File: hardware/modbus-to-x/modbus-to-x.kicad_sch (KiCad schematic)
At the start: 33 parts, among them J1 PWR, J2 UART, SW1 SW_Push, SW2 SW_Push, U1 AMS1117-3.3, U3 MAX3485, U4 ESP32-WROOM-32D, U5 AT24CS64-XHM, U6 AT24CS64-XHM, U7 LMR14020SQDPRTQ1

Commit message: updated hw
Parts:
- removed C1: 4.7uF/25V, Capacitor_SMD:C_0805_2012Metric_Pad1.18x1.45mm_HandSolder, symbol Device:C
- removed C12: 47uF, ~, symbol SparkFun-Capacitor:C_Polarized
- removed C9: 22uF/10V(20%), Capacitor_SMD:C_0402_1005Metric_Pad0.74x0.62mm_HandSolder, symbol Device:C
- added C1: 47uF, Capacitor_SMD:CP_Elec_6.3x5.4, symbol Device:C_Polarized
- added C12, C21: 100pF, Capacitor_SMD:C_0805_2012Metric_Pad1.18x1.45mm_HandSolder, symbol Device:C
- added C13, C14, C16, C17, C18, C2: 10uF, Capacitor_SMD:C_0805_2012Metric_Pad1.18x1.45mm_HandSolder, symbol Device:C
- added C15: 22uF, Capacitor_SMD:C_0805_2012Metric_Pad1.18x1.45mm_HandSolder, symbol Device:C
- added C19: 0.01uF, Capacitor_SMD:C_0402_1005Metric_Pad0.74x0.62mm_HandSolder, symbol Device:C
- added C20: 2.2nF, Capacitor_SMD:C_0805_2012Metric_Pad1.18x1.45mm_HandSolder, symbol Device:C
- added C22: 0.1uF, Capacitor_SMD:C_1206_3216Metric_Pad1.33x1.80mm_HandSolder, symbol Device:C
- added D3: SMAJ12A, Diode_SMD:D_SMA_Handsoldering, symbol Diode:SMAJ12A
- added L2: MPZ1005S121CT000, MPZ1005S121CT000:IND_1005_TDK-L, symbol MPZ1005S121CT000:MPZ1005S121CT000
- added R10: 47k, Resistor_SMD:R_0805_2012Metric_Pad1.20x1.40mm_HandSolder, symbol Device:R
- added R11: 22K, Resistor_SMD:R_0603_1608Metric_Pad0.98x0.95mm_HandSolder, symbol Device:R
- added R12: 620R, Resistor_SMD:R_0805_2012Metric_Pad1.20x1.40mm_HandSolder, symbol Device:R
- C10: FriendlyName (none) -> CBoot; PartNo (none) -> CC0402MRX5R7BB104; Voltage (none) -> 16V
- C11: value 4.7uF -> 2.2nF; footprint Capacitor_SMD:C_0402_1005Metric_Pad0.74x0.62mm_HandSolder -> Capacitor_SMD:C_0805_2012Metric_Pad1.18x1.45mm_HandSolder; FriendlyName (none) -> Css; PartNo (none) -> RND 1500805B222J500NT; Voltage (none) -> 50V
- C3: value 0.1uF/50V(10%) -> 22uF; footprint Capacitor_SMD:C_0402_1005Metric_Pad0.74x0.62mm_HandSolder -> Capacitor_SMD:C_0805_2012Metric_Pad1.18x1.45mm_HandSolder; ProductCode (none) -> CL21A226MOCLRNC; now left out of the parts list
- C4, C5, C7: value 0.1uF/50V(10%) -> 0.1uF; footprint Capacitor_SMD:C_0402_1005Metric_Pad0.74x0.62mm_HandSolder -> Capacitor_SMD:C_1206_3216Metric_Pad1.33x1.80mm_HandSolder; ProductCode (none) -> CVNF100K12X; now left out of the parts list
- C6, C8: value 22uF/10V(20%) -> 22uF; footprint Capacitor_SMD:C_0402_1005Metric_Pad0.74x0.62mm_HandSolder -> Capacitor_SMD:C_0805_2012Metric_Pad1.18x1.45mm_HandSolder; ProductCode (none) -> CL21A226MOCLRNC; now left out of the parts list
- D1, J1, J2, R2, R3, R4, R5, SW1, SW2, U1, U3, U4, U5, U6: now left out of the parts list
- D2: value MBR0530 -> MBRS340T3G; footprint Diode_SMD:D_SOD-123 -> Diode_SMD:D_SMB-SMC_Universal_Handsoldering; PartNo (none) -> MBRS340T3G
- L1: value 5.5uH -> 4.7uH; footprint SparkFun-Capacitor:C_0805_2012Metric -> WE 74404041047:L_Wurth_WE-LQS-4012; PROD_ID NDUC- -> (none); PartNo (none) -> WE 74404041047
- R1: footprint (none) -> Resistor_SMD:R_1206_3216Metric_Pad1.30x1.75mm_HandSolder; ProductCode (none) -> 1551206S4F1000T5E; now left out of the parts list
- R6: PartNo (none) -> 155TC0525B1002T5J
- R7: value 23.2K -> 620R; FriendlyName (none) -> Rt; PartNo (none) -> 1550805S8F6200T5E
- R8: value 10K -> 390k; footprint Resistor_SMD:R_0805_2012Metric_Pad1.20x1.40mm_HandSolder -> Resistor_SMD:R_0402_1005Metric_Pad0.72x0.64mm_HandSolder; FriendlyName (none) -> Rfbt
- R9: value 10K -> 22k; footprint Resistor_SMD:R_0805_2012Metric_Pad1.20x1.40mm_HandSolder -> Resistor_SMD:R_0603_1608Metric_Pad0.98x0.95mm_HandSolder; FriendlyName (none) -> Rfbb2
- U7: footprint DPR0010A -> LMR14020SQDPRTQ1:DPR0010A
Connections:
- net EN: now also C4.1, C22.1; no longer C3.2, C5.2
- net GND: now also C3.2, C4.2, C5.2, R9.1, C1.2, C13.1, C14.1, C15.1, C16.1, C17.1, C18.1, C19.2, C2.1, C20.1, C22.2, D3.2 (A2), R11.1; no longer C3.1, C4.1, C5.1, R7.1
- net IO_0: now also C5.1; no longer C4.2
- net VBUS_12: now also U7.4 (EN), C1.1, C16.2, C17.2, C18.2, C19.1, L2.1; no longer J1.1 (Pin_1)
- net VCC5: now also C12.2, C13.2, C14.2, C15.2, C2.2, C21.2
- net VDD33: now also C3.1
- net at U7.5 (RT_SYNC): now also R12.1; no longer R7.2
- net at C11.2, U7.6 (SS): now also C20.2
- net at U7.7 (FB): now also R8.2, C12.1, C21.1, R10.2; no longer R9.1
- net at R9.2: now also R10.1; no longer R8.2
- new net: D3.1 (A1), J1.1 (Pin_1), L2.2
- new net: R12.2, R7.2
- new net: R11.2, R7.1
- no-connect marks 29 -> 28
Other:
- note added: "12V Input"
- note added: "3v3 Linear Voltage Regulator"
- note added: "Cff"
- note added: "Cin Caps"
- note added: "Cout Caps"
- note added: "Css"
- note added: "Rfbb"
- note added: "Rt"
- note added: "UART"
- note removed: "Peripherals"
- moved on the sheet: C6, C7, C8, D1, D2, J1, J2, L1, R1, R2, R3, R4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

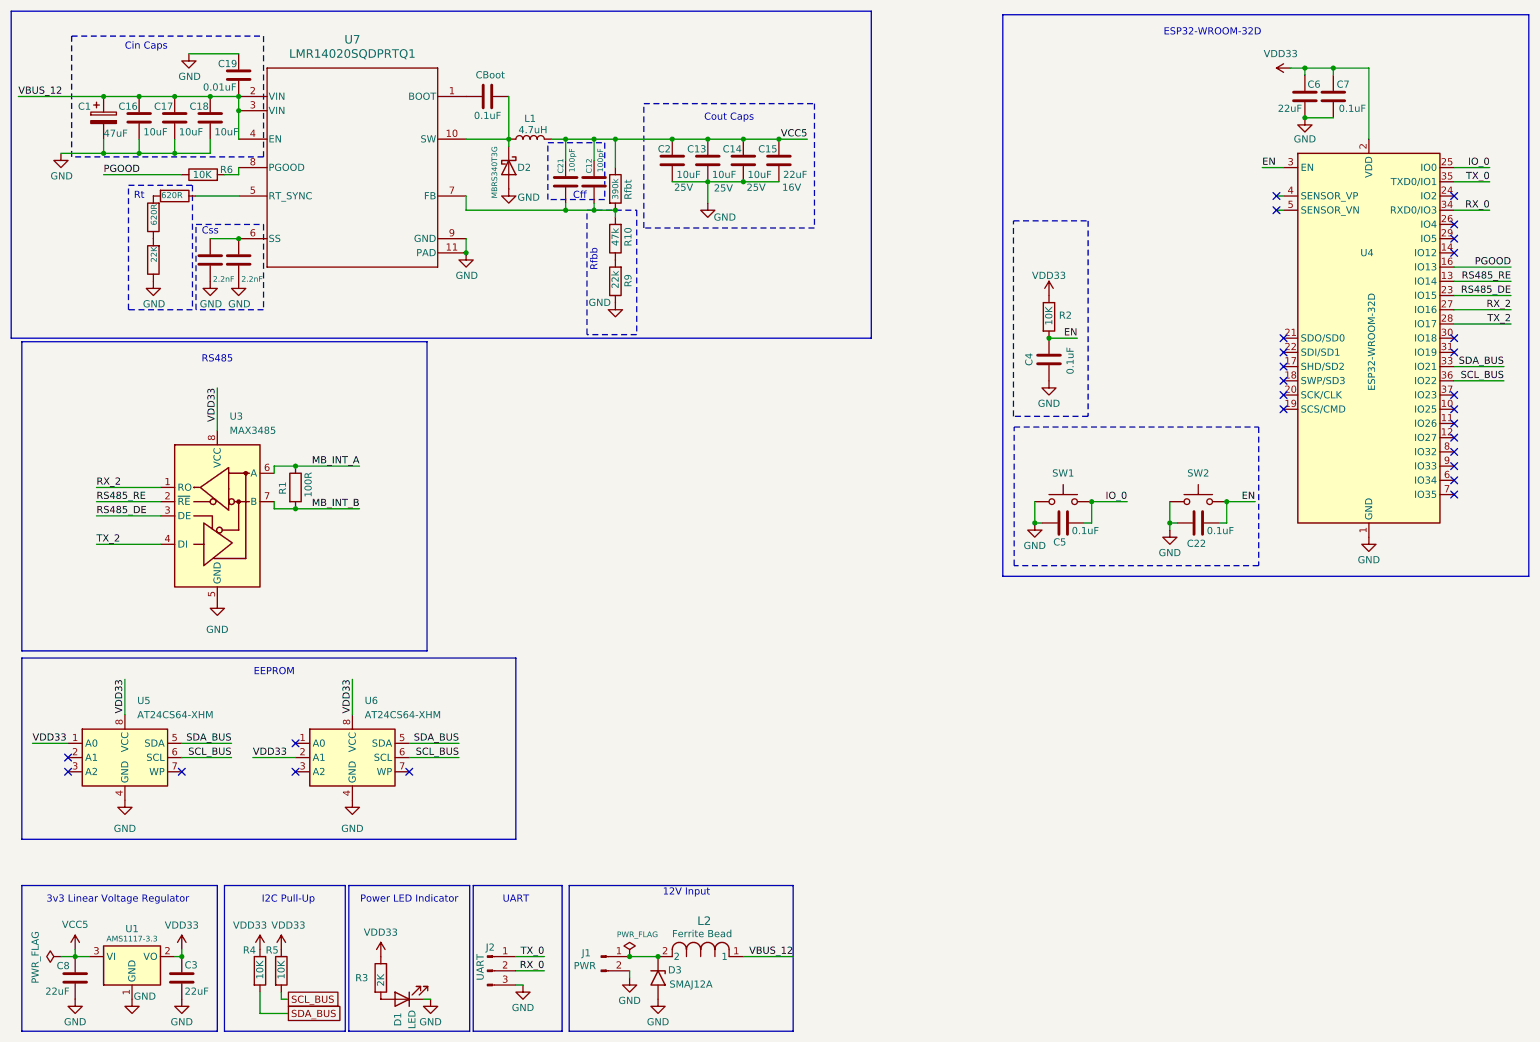
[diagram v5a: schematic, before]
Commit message: updated footprints
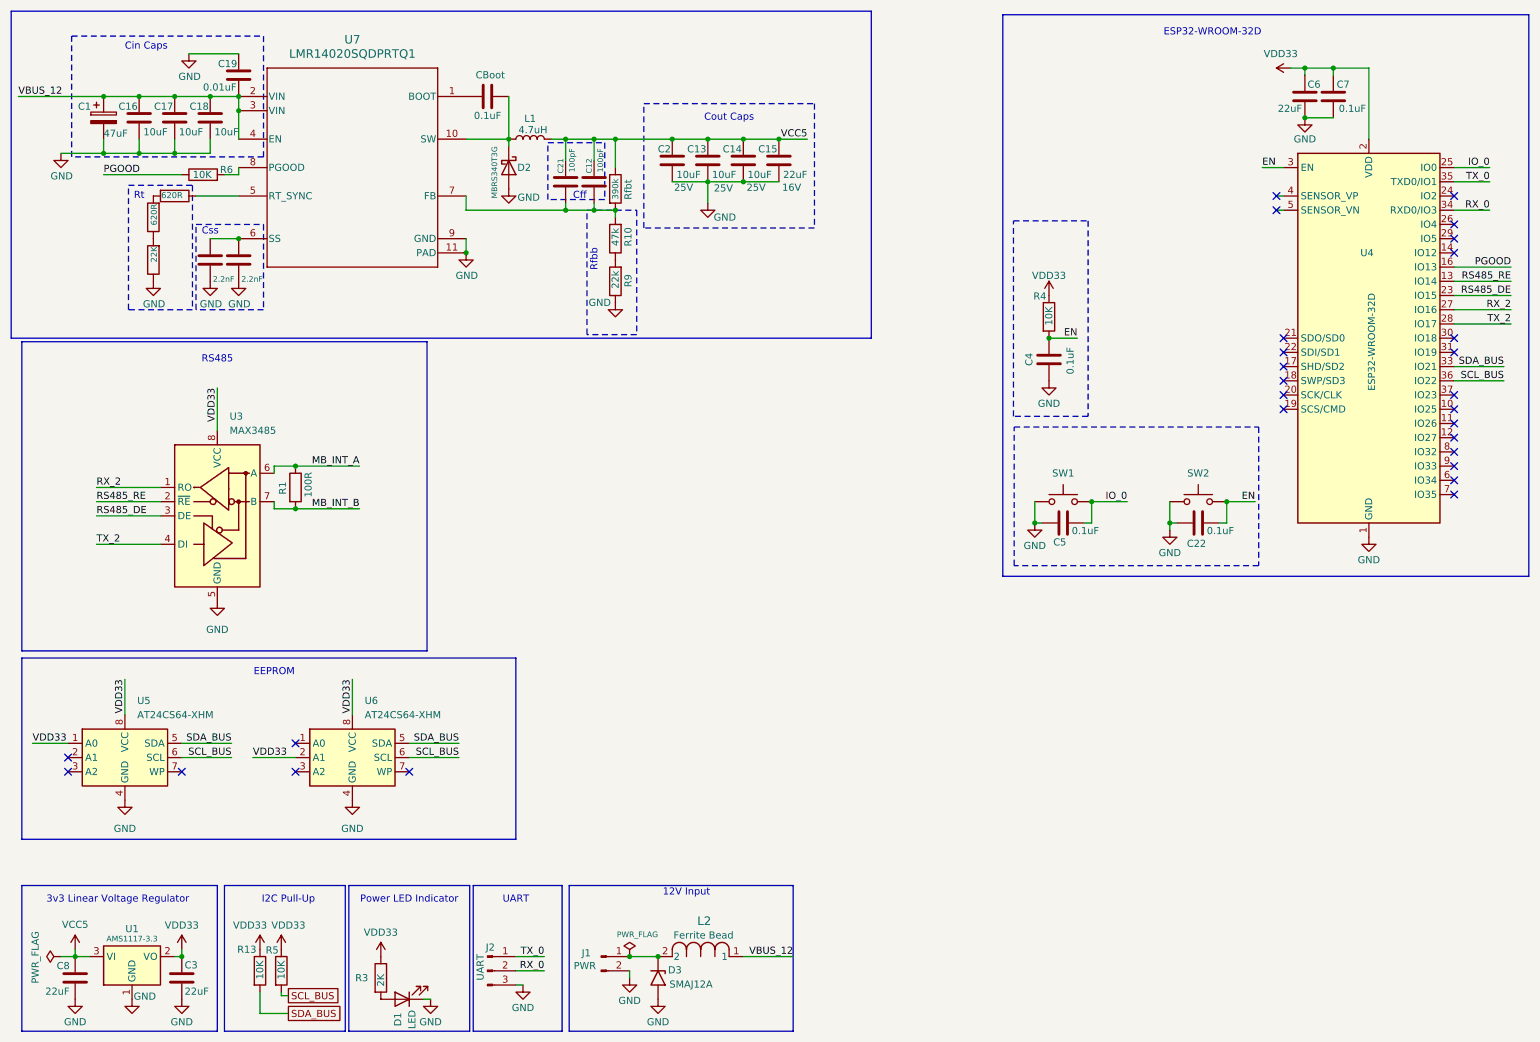
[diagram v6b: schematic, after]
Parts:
- removed R2: 10K, Resistor_SMD:R_0805_2012Metric_Pad1.20x1.40mm_HandSolder, symbol Device:R
- added R13: 10K, Resistor_SMD:R_0805_2012Metric_Pad1.20x1.40mm_HandSolder, symbol Device:R
- C1: FriendlyName (none) -> Cout47uf; PartNo (none) -> CSMK047/35; ProductCode CSMK047/35 -> (none)
- C12: FriendlyName Cff2 -> Cff; PartNo (none) -> RND 1500805N101J500NT; ProductCode RND 1500805N101J500NT -> (none)
- C13, C14, C16, C17, C18, C2: FriendlyName Cout -> Cout10uf
- C15: FriendlyName Cout -> Cout22uf
- C19: FriendlyName Cout -> Cin0_1uf
- C21: FriendlyName Cff1 -> Cff; PartNo (none) -> RND 1500805N101J500NT; ProductCode RND 1500805N101J500NT -> (none)
- C22, C4, C5, C7: PartNo (none) -> CVNF100K12X; ProductCode CVNF100K12X -> (none); Voltage (none) -> 50V
- C3, C6, C8: PartNo (none) -> CL21A226MOCLRNC; ProductCode CL21A226MOCLRNC -> (none); Voltage (none) -> 16V
- D1: PartNo (none) -> LW QH8G-Q2OO-3K5L-1
- L2: FriendlyName (none) -> Ferrite Bead
- R1: PartNo (none) -> 1551206S4F1000T5E; ProductCode 1551206S4F1000T5E -> (none)
- R10: FriendlyName Rfbb1 -> Rfbb_47k
- R3: footprint Resistor_SMD:R_0805_2012Metric_Pad1.20x1.40mm_HandSolder -> Resistor_SMD:R_0603_1608Metric_Pad0.98x0.95mm_HandSolder; PartNo (none) -> RND 155TC0325B2001T5H
- R4, R5: PartNo (none) -> RND 155TC0525B1002T5J
- R8: PartNo (none) -> RC0402FR-07390KL
- R9: FriendlyName Rfbb2 -> Rfbb22k
- U3: PartNo (none) -> MAX485
- U4: PartNo (none) -> M113DH2800PH3Q0
- U7: PartNo (none) -> LMR14020Q
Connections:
- net EN: now also R4.2
- net SDA_BUS: now also R13.2; no longer R4.2
- net VDD33: now also R13.1
